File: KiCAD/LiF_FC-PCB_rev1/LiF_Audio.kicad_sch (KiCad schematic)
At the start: 24 parts, among them J33 Amp V select, J34 ST 1 Bypass, J35 ST 2 Bypass, J36 Vol Pot Bypass, J37 SKP OUT, U12 PAM8302AAS

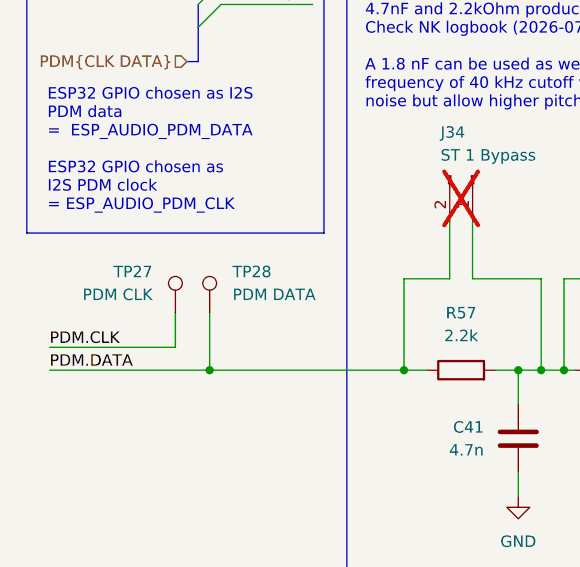
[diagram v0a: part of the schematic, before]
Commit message: finished service PCB routing and silkscreen, finished IO PCB layout, routing, and silkscreen. Exported production files, submitted PCB for manufacturing by JLCPCB
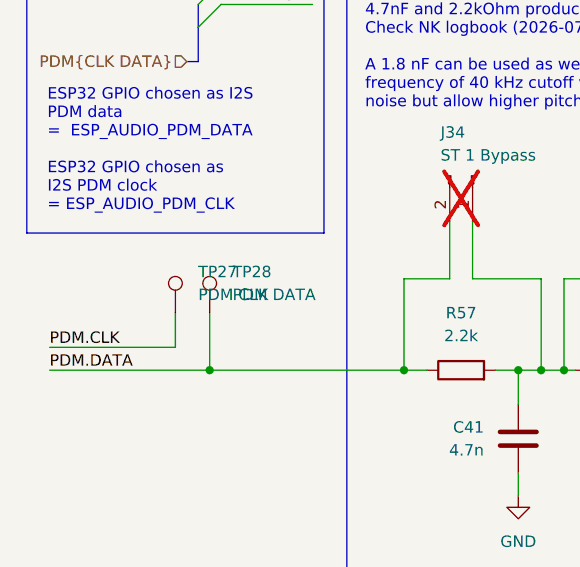
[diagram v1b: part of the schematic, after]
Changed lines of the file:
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@@
 		(lib_id "Connector:TestPoint")
 		(at 33.02 125.73 0)
-		(mirror y)
 		(unit 1)
 		(exclude_from_sim no)
@@
 		(dnp no)
 		(property "Reference" "TP27"
-			(at 30.48 121.1579 0)
+			(at 35.56 121.1579 0)
 			(effects
 				(font
@@
 		)
 		(property "Value" "PDM CLK"
-			(at 30.48 123.6979 0)
+			(at 35.56 123.6979 0)
 			(effects
 				(font
@@
 		)
 		(property "Footprint" "TestPoint:TestPoint_Loop_D1.80mm_Drill1.0mm_Beaded"
-			(at 27.94 125.73 0)
+			(at 38.1 125.73 0)
 			(effects
 				(font
@@
 		)
 		(property "Datasheet" "~"
-			(at 27.94 125.73 0)
+			(at 38.1 125.73 0)
 			(effects
 				(font
